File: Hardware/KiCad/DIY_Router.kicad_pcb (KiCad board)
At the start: 2 copper layers, 22 parts, among them IC1 HLK-7628N, IC2 TPS62A06ADRLR, J1 217179-0001, J2 RJ45_Hanrun_HR911105A_Horizon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, J3 RJ45_Hanrun_HR911105A_Horizon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, J4 RJ45_Hanrun_HR911105A_Horizon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

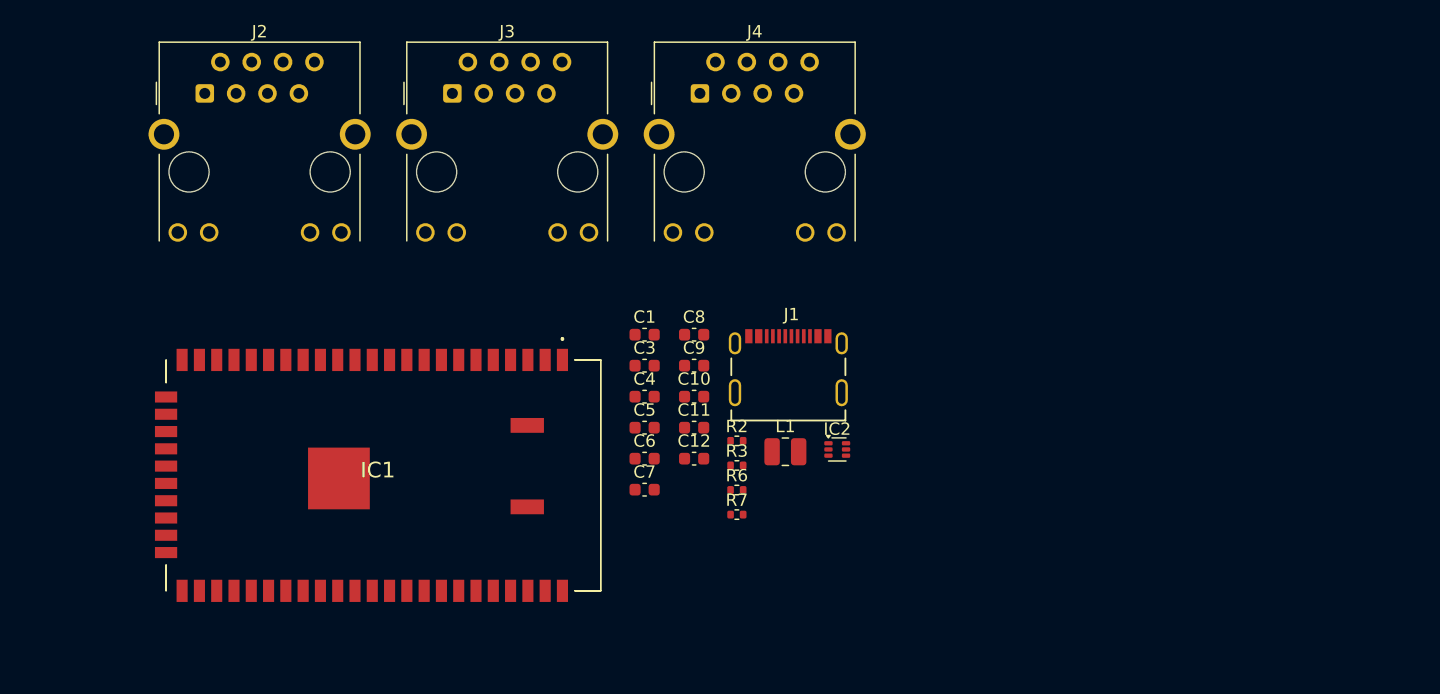
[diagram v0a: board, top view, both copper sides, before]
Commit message: USB_Bridge: add transformerless connection between usb bridge and SOM
- Ethernet: Add fourth rj45 jack
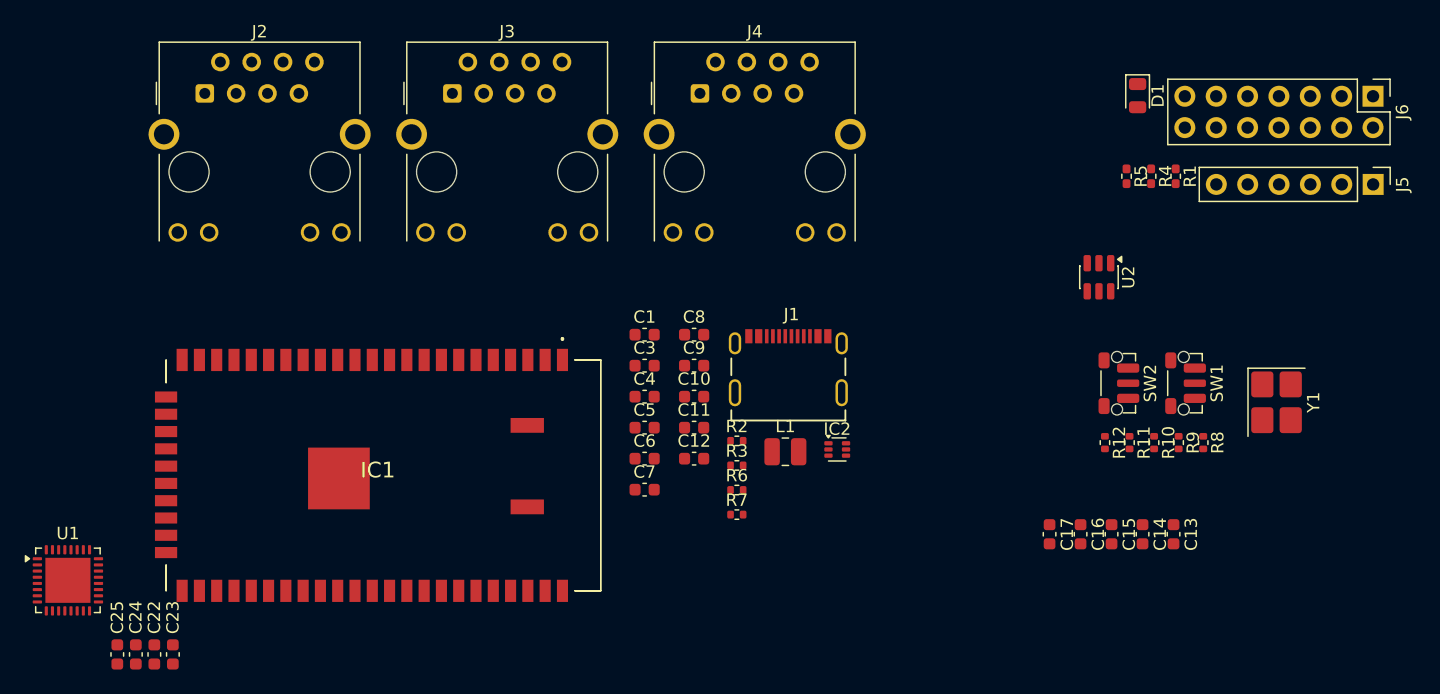
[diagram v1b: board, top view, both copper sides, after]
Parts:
- added C13: 100nF, Capacitor_SMD:C_0603_1608Metric, F.Cu at (143.5, 69.3)
- added C14: 100nF, Capacitor_SMD:C_0603_1608Metric, F.Cu at (141.0, 69.3)
- added C15: 4.7µF, Capacitor_SMD:C_0603_1608Metric, F.Cu at (138.5, 69.3)
- added C16: 18pF, Capacitor_SMD:C_0603_1608Metric, F.Cu at (136.0, 69.3)
- added C17: 18pF, Capacitor_SMD:C_0603_1608Metric, F.Cu at (133.5, 69.3)
- added C22: 100nF, Capacitor_SMD:C_0603_1608Metric, F.Cu at (61.0, 79.0)
- added C23: 100nF, Capacitor_SMD:C_0603_1608Metric, F.Cu at (62.5, 79.0)
- added C24: 100nF, Capacitor_SMD:C_0603_1608Metric, F.Cu at (59.5, 79.0)
- added C25: 100nF, Capacitor_SMD:C_0603_1608Metric, F.Cu at (58.0, 79.0)
- added D1: LED, LED_SMD:LED_0805_2012Metric, F.Cu at (140.6, 33.7)
- added J5: Conn_01x06_Pin, Connector_PinHeader_2.54mm:PinHeader_1x06_P2.54mm_Vertical, F.Cu at (159.7, 40.9)
- added J6: Conn_02x07_Odd_Even, Connector_PinHeader_2.54mm:PinHeader_2x07_P2.54mm_Vertical, F.Cu at (159.7, 33.8)
- added R1: 1k, Resistor_SMD:R_0402_1005Metric_Pad0.72x0.64mm_HandSolder, F.Cu at (143.7, 40.3)
- added R10: 10k, Resistor_SMD:R_0402_1005Metric, F.Cu at (142.0, 61.8)
- added R11: 226 1%, Resistor_SMD:R_0402_1005Metric, F.Cu at (140.0, 61.8)
- added R12: 220, Resistor_SMD:R_0402_1005Metric, F.Cu at (138.0, 61.8)
- added R4: 1k, Resistor_SMD:R_0402_1005Metric_Pad0.72x0.64mm_HandSolder, F.Cu at (141.7, 40.3)
- added R5: 1k, Resistor_SMD:R_0402_1005Metric_Pad0.72x0.64mm_HandSolder, F.Cu at (139.7, 40.3)
- added R8: 1M, Resistor_SMD:R_0402_1005Metric, F.Cu at (145.9, 61.8)
- added R9: 10k, Resistor_SMD:R_0402_1005Metric, F.Cu at (144.0, 61.8)
- added SW1: SW_Push, Button_Switch_SMD:SW_Push_1P1T-MP_NO_Horizontal_Alps_SKRTLAE010, F.Cu at (144.4, 57.0)
- added SW2: SW_Push, Button_Switch_SMD:SW_Push_1P1T-MP_NO_Horizontal_Alps_SKRTLAE010, F.Cu at (139.0, 57.0)
- added U1: XR22801IL32TR-F, Package_DFN_QFN:QFN-32-1EP_5x5mm_P0.5mm_EP3.65x3.65mm, F.Cu at (54.0, 73.0)
- added U2: USBLC6-2SC6Y, Package_TO_SOT_SMD:SOT-23-6, F.Cu at (137.5, 48.5)
- added Y1: ABM8-25.000MHZ-B2-T3, Crystal:Crystal_SMD_3225-4Pin_3.2x2.5mm_HandSoldering, F.Cu at (151.9, 58.6)
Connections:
- IC1 pad 10: unconnected-(IC1-EPHY_LED3-Pad10) -> EPHY_LED3
- IC1 pad 11: unconnected-(IC1-EPHY_LED2-Pad11) -> EPHY_LED2
- IC1 pad 12: unconnected-(IC1-EPHY_LED1-Pad12) -> EPHY_LED1
- IC1 pad 13: unconnected-(IC1-EPHY_LED0-Pad13) -> EPHY_LED0
- IC1 pad 14: Net-(IC1-PORST_N) -> CPU_RST
- IC1 pad 15: unconnected-(IC1-UART_TXD1-Pad15) -> UART_TXD1
- IC1 pad 16: unconnected-(IC1-UART_RXD1-Pad16) -> UART_RXD1
- IC1 pad 24: unconnected-(IC1-I2C_SCLK-Pad24) -> /DIY_Router/I2C_SCL
- IC1 pad 25: unconnected-(IC1-I2C_SD-Pad25) -> /DIY_Router/I2C_SDA
- IC1 pad 26: unconnected-(IC1-SPI_CS1-Pad26) -> /DIY_Router/SPI_CS1
- IC1 pad 27: unconnected-(IC1-SPI_CLK-Pad27) -> /DIY_Router/SPI_CLK
- IC1 pad 28: unconnected-(IC1-SPI_MISO-Pad28) -> /DIY_Router/SPI_MISO
- IC1 pad 29: unconnected-(IC1-SPI_MOSI-Pad29) -> /DIY_Router/SPI_MOSI
- IC1 pad 30: unconnected-(IC1-GPIO0-Pad30) -> /DIY_Router/GPIO0
- IC1 pad 31: unconnected-(IC1-UART_TXD0-Pad31) -> UART_TXD0
- IC1 pad 32: unconnected-(IC1-UART_RXD0-Pad32) -> UART_RXD0
- IC1 pad 5: unconnected-(IC1-SPI_CS0-Pad5) -> /DIY_Router/SPI_CS0
- IC1 pad 8: unconnected-(IC1-WDT_RST_N-Pad8) -> WDT_RST
- IC1 pad 9: unconnected-(IC1-EPHY_LED4-Pad9) -> EPHY_LED4
- J1 pad A6: unconnected-(J1-D+-PadA6) -> USB_C_DP
- J1 pad A7: unconnected-(J1-D--PadA7) -> USB_C_DN
- J1 pad B6: unconnected-(J1-D+-PadB6) -> USB_C_DP
- J1 pad B7: unconnected-(J1-D--PadB7) -> USB_C_DN
- J2 pad 10: unconnected-(J2-Pad10) -> EPHY_LED0
- J2 pad 9: unconnected-(J2-Pad9) -> Net-(J2-Pad9)
- J3 pad 10: unconnected-(J3-Pad10) -> EPHY_LED1
- J3 pad 9: unconnected-(J3-Pad9) -> Net-(J3-Pad9)
- J4 pad 10: unconnected-(J4-Pad10) -> EPHY_LED2
- J4 pad 9: unconnected-(J4-Pad9) -> Net-(J4-Pad9)

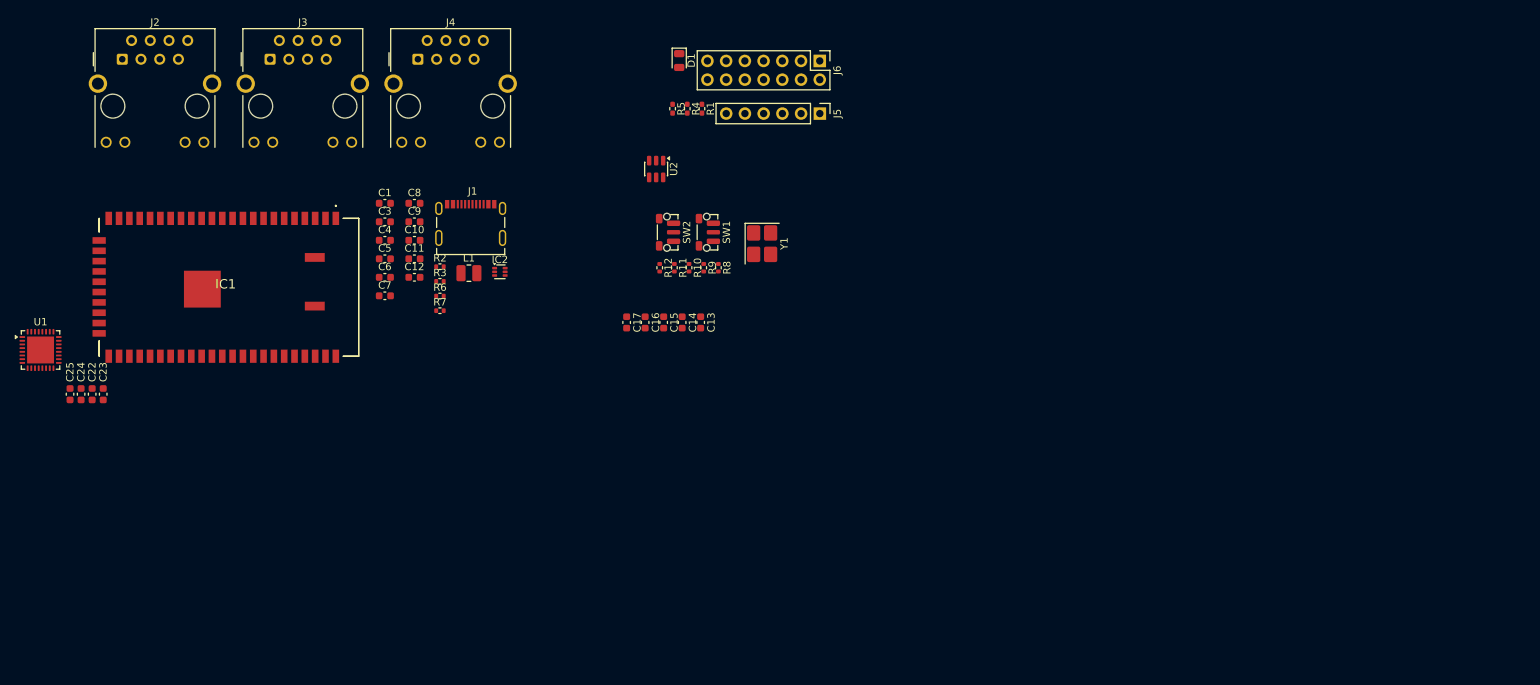
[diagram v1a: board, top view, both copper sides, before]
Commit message: Fix footprints for Mini PCIe and switches (set pads for mounting and case to GND) Set PCB to 4 layer with 0.5 OZ (0,017mm) copper on the inner layers Start sorting the footprints on the PCB TO-DO: check footprints of Y1 and Y2, they seem way too large
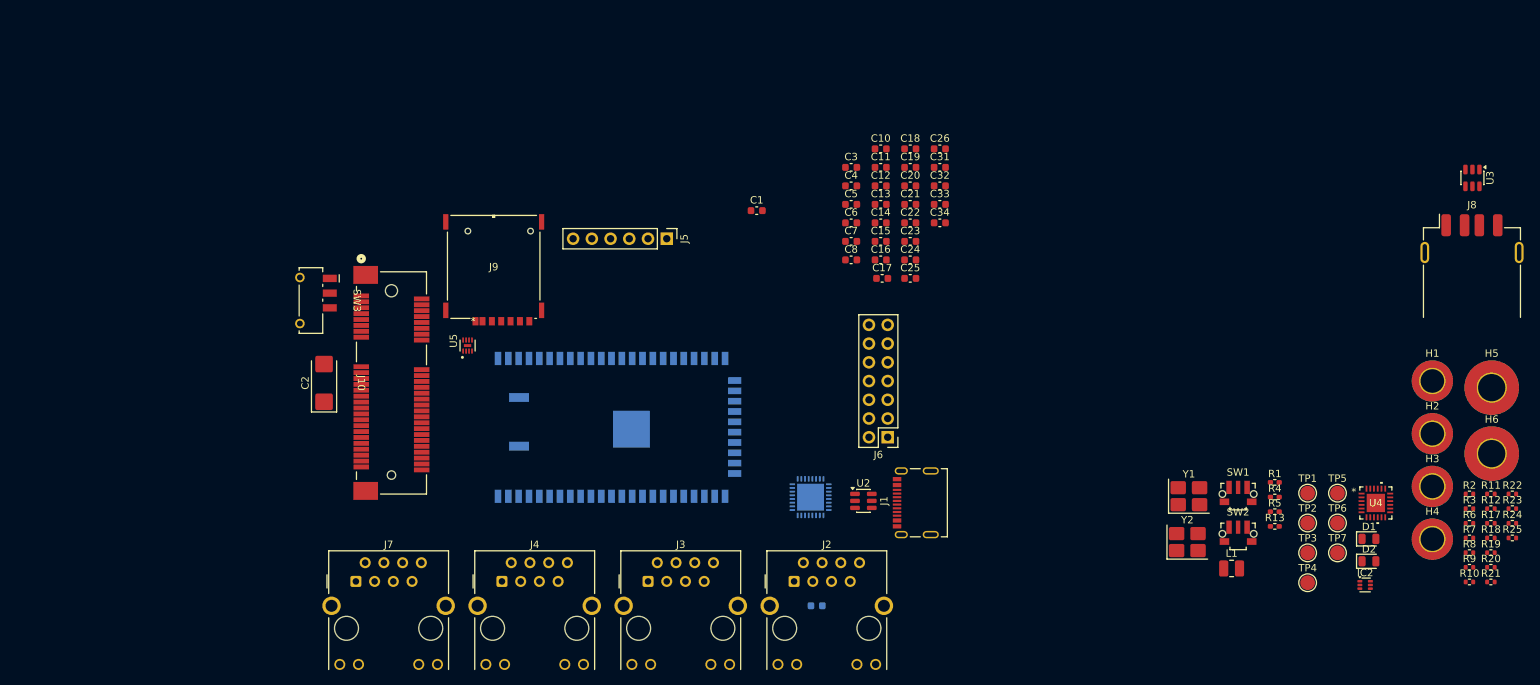
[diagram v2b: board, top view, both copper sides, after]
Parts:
- added C18: 100nF, Capacitor_SMD:C_0603_1608Metric, F.Cu at (172.0, 45.7)
- added C19: 100nF, Capacitor_SMD:C_0603_1608Metric, F.Cu at (172.0, 48.2)
- added C2: 470µF, Capacitor_Tantalum_SMD:CP_EIA-6032-28_Kemet-C_HandSolder, F.Cu at (92.5, 77.5)
- added C20: 18pF, Capacitor_SMD:C_0603_1608Metric, F.Cu at (172.0, 50.7)
- added C21: 18pF, Capacitor_SMD:C_0603_1608Metric, F.Cu at (172.0, 53.2)
- added C26: 100nF, Capacitor_SMD:C_0603_1608Metric, F.Cu at (176.0, 45.7)
- added C31: 100nF, Capacitor_SMD:C_0603_1608Metric, F.Cu at (176.0, 48.2)
- added C32: 1pF, Capacitor_SMD:C_0603_1608Metric, F.Cu at (176.0, 50.7)
- added C33: 100nF, Capacitor_SMD:C_0603_1608Metric, F.Cu at (176.0, 53.2)
- added C34: 1µF, Capacitor_SMD:C_0603_1608Metric, F.Cu at (176.0, 55.8)
- added D2: LED, LED_SMD:LED_0805_2012Metric, F.Cu at (234.2, 101.7)
- added H1: MountingHole_Pad, MountingHole:MountingHole_3.2mm_M3_DIN965_Pad_TopBottom, F.Cu at (242.8, 77.2)
- added H2: MountingHole_Pad, MountingHole:MountingHole_3.2mm_M3_DIN965_Pad_TopBottom, F.Cu at (242.8, 84.4)
- added H3: MountingHole_Pad, MountingHole:MountingHole_3.2mm_M3_DIN965_Pad_TopBottom, F.Cu at (242.8, 91.5)
- added H4: MountingHole_Pad, MountingHole:MountingHole_3.2mm_M3_DIN965_Pad_TopBottom, F.Cu at (242.8, 98.7)
- added H5: MountingHole_Pad, MountingHole:MountingHole_3.7mm_Pad_TopBottom, F.Cu at (250.8, 78.1)
- added H6: MountingHole_Pad, MountingHole:MountingHole_3.7mm_Pad_TopBottom, F.Cu at (250.8, 87.1)
- added J10: 2041262-1, TE_2041262:CONN60_2041262-1_TEC, F.Cu at (101.6, 77.5)
- added J7: RJ45_Hanrun_HR911105A_Horizontal, Connector_RJ:RJ45_Hanrun_HR911105A_Horizontal, F.Cu at (96.8, 104.4)
- added J8: USB_A, Connector_USB:USB_A_Receptacle_GCT_USB1046, F.Cu at (248.2, 63.3)
- added J9: SIM8066-6-1-14-01-A, SIM8066_6:CONN_SIM8066-6-1-14-01-A_GCT, F.Cu at (115.5, 61.7)
- added R13: 1k, Resistor_SMD:R_0402_1005Metric_Pad0.72x0.64mm_HandSolder, F.Cu at (221.4, 96.9)
- added R17: 15k, Resistor_SMD:R_0402_1005Metric, F.Cu at (250.7, 96.5)
- added R18: 12k 1%, Resistor_SMD:R_0402_1005Metric, F.Cu at (250.7, 98.5)
- added R19: 220, Resistor_SMD:R_0402_1005Metric, F.Cu at (250.7, 100.5)
- added R20: 50k, Resistor_SMD:R_0402_1005Metric, F.Cu at (250.7, 102.5)
- added R21: 50k, Resistor_SMD:R_0402_1005Metric, F.Cu at (250.7, 104.5)
- added R22: 50k, Resistor_SMD:R_0402_1005Metric, F.Cu at (253.6, 92.5)
- added R23: 10k, Resistor_SMD:R_0402_1005Metric, F.Cu at (253.6, 94.5)
- added R24: 100k, Resistor_SMD:R_0402_1005Metric, F.Cu at (253.6, 96.5)
- added R25: 100k, Resistor_SMD:R_0402_1005Metric, F.Cu at (253.6, 98.5)
- added SW3: 450405020524, WS-SLSU:SW_Wurth_WS-SLSU_450405020524, F.Cu at (90.7, 66.3)
- added TP1: TestPoint, TestPoint:TestPoint_Pad_D2.0mm, F.Cu at (225.9, 92.4)
- added TP2: TestPoint, TestPoint:TestPoint_Pad_D2.0mm, F.Cu at (225.9, 96.5)
- added TP3: TestPoint, TestPoint:TestPoint_Pad_D2.0mm, F.Cu at (225.9, 100.5)
- added TP4: TestPoint, TestPoint:TestPoint_Pad_D2.0mm, F.Cu at (225.9, 104.6)
- added TP5: TestPoint, TestPoint:TestPoint_Pad_D2.0mm, F.Cu at (229.9, 92.4)
- added TP6: TestPoint, TestPoint:TestPoint_Pad_D2.0mm, F.Cu at (229.9, 96.5)
- added TP7: TestPoint, TestPoint:TestPoint_Pad_D2.0mm, F.Cu at (229.9, 100.5)
- added U3: USBLC6-2SC6Y, Package_TO_SOT_SMD:SOT-23-6, F.Cu at (248.2, 49.7)
- added U4: USB2422T/MJ, USB2422T_MJ:SQFN24_4X4MC_MCH, F.Cu at (235.1, 93.8)
- added U5: EMIF03-SIM02M8, EMIF03-SIM02M8:SON40P170X150X60-9N, F.Cu at (111.9, 72.4)
- added Y2: ABM8-24.000MHZ-B2-T, Crystal:Crystal_SMD_3225-4Pin_3.2x2.5mm_HandSoldering, F.Cu at (209.6, 99.1)
- C9, IC1, U1: moved to B.Cu
- J1: value 217179-0001 -> 2171790001
- SW1, SW2: value SW_Push -> 436333033816; footprint Button_Switch_SMD:SW_Push_1P1T-MP_NO_Horizontal_Alps_SKRTLAE010 -> WS-TASU:SW_Wurth_WS-TASU_436333033816
- moved R2 143.0 mm to (247.8, 92.5)
- moved R3 143.0 mm to (247.8, 94.5)
- moved R6 143.0 mm to (247.8, 96.5)
- moved R7 143.0 mm to (247.8, 98.5)
- moved IC2 124.8 mm to (233.7, 104.9)
- moved R12 117.4 mm to (250.7, 94.5), turned to 0 degrees
- moved J2 115.4 mm to (156.2, 104.4)
- moved C25 115.0 mm to (172.0, 63.3), turned to 0 degrees
- moved R11 114.9 mm to (250.7, 92.5), turned to 0 degrees
- moved R10 114.1 mm to (247.8, 104.5), turned to 0 degrees
- moved C24 113.9 mm to (172.0, 60.8), turned to 0 degrees
- moved D1 113.9 mm to (234.2, 98.6), turned to 0 degrees
- moved C22 113.4 mm to (172.0, 55.8), turned to 0 degrees
- moved R9 111.5 mm to (247.8, 102.5), turned to 0 degrees
- moved C23 111.4 mm to (172.0, 58.3), turned to 0 degrees
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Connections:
- C10 pad 1: Net-(J3-RCT) -> Net-(J2-RCT)
- C11 pad 1: Net-(J4-TCT) -> Net-(J3-TCT)
- C12 pad 1: Net-(J4-RCT) -> Net-(J3-RCT)
- C7 pad 1: Net-(J2-TCT) -> Net-(J4-TCT)
- C8 pad 1: Net-(J2-RCT) -> Net-(J4-RCT)
- C9 pad 1: Net-(J3-TCT) -> Net-(J2-TCT)
- IC1 pad 46: unconnected-(IC1-MDI_TP_P3-Pad46) -> MDI_TP_P3
- IC1 pad 47: unconnected-(IC1-MDI_TN_P3-Pad47) -> MDI_TN_P3
- IC1 pad 48: unconnected-(IC1-MDI_RP_P3-Pad48) -> MDI_RP_P3
- IC1 pad 49: unconnected-(IC1-MDI_RN_P3-Pad49) -> MDI_RN_P3
- IC1 pad 50: unconnected-(IC1-MDI_RP_P4-Pad50) -> MDI_RP_P4
- IC1 pad 51: unconnected-(IC1-MDI_RN_P4-Pad51) -> MDI_RN_P4
- IC1 pad 52: unconnected-(IC1-MDI_TP_P4-Pad52) -> MDI_TP_P4
- IC1 pad 53: unconnected-(IC1-MDI_TN_P4-Pad53) -> MDI_TN_P4
- IC1 pad 54: unconnected-(IC1-USB_DP-Pad54) -> SOM_USB_DP
- IC1 pad 55: unconnected-(IC1-USB_DM-Pad55) -> SOM_USB_DN
- J1 pad A1B12: (no net) -> Net-(J1-CC2)
- J1 pad A4B9: (no net) -> VBUS
- J1 pad B1A12: (no net) -> Net-(J1-CC2)
- J1 pad B4A9: (no net) -> VBUS
- J1 pad SH1: (no net) -> Net-(J1-CC2)
- J1 pad SH2: (no net) -> Net-(J1-CC2)
- J1 pad SH3: (no net) -> Net-(J1-CC2)
- J1 pad SH4: (no net) -> Net-(J1-CC2)
- J2 pad 1: MDI_TP_P0 -> MDI_TP_P1
- J2 pad 10: EPHY_LED0 -> EPHY_LED1
- J2 pad 2: MDI_TN_P0 -> MDI_TN_P1
- J2 pad 3: MDI_RP_P0 -> MDI_RP_P1
- J2 pad 6: MDI_RN_P0 -> MDI_RN_P1
- J3 pad 1: MDI_TP_P1 -> MDI_TP_P2
- J3 pad 10: EPHY_LED1 -> EPHY_LED2
- J3 pad 2: MDI_TN_P1 -> MDI_TN_P2
- J3 pad 3: MDI_RP_P1 -> MDI_RP_P2
- J3 pad 6: MDI_RN_P1 -> MDI_RN_P2
- J4 pad 1: MDI_TP_P2 -> MDI_TP_P3
- J4 pad 10: EPHY_LED2 -> EPHY_LED3
- J4 pad 2: MDI_TN_P2 -> MDI_TN_P3
- J4 pad 3: MDI_RP_P2 -> MDI_RP_P3
- J4 pad 6: MDI_RN_P2 -> MDI_RN_P3
- R1 pad 2: Net-(J2-Pad9) -> Net-(J4-Pad9)
- R4 pad 2: Net-(J3-Pad9) -> Net-(J2-Pad9)
- R5 pad 2: Net-(J4-Pad9) -> Net-(J3-Pad9)
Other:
- copper layers 2 -> 4
